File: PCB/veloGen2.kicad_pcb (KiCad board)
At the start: 2 copper layers, 67 x 24 mm, 43 parts, among them J1 Conn_01x06, J2 Gen. IN, J3 Bat, Q3 STL6N3LLH6, T1 MSD1260, U1 ESP-WROOM-32, U2 TS1101, U4 MAX8881, U5 MCP1630

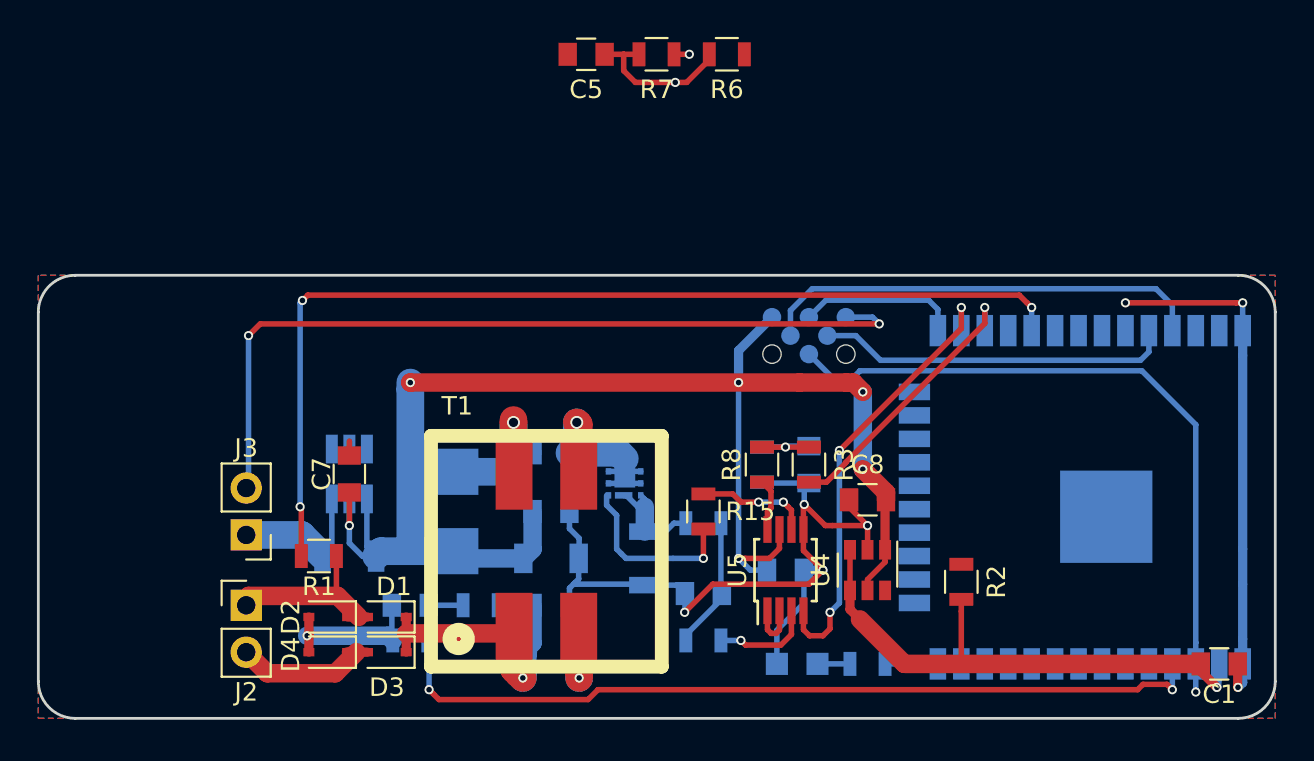
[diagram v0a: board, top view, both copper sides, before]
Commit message: moved stuff around 0.6 vias
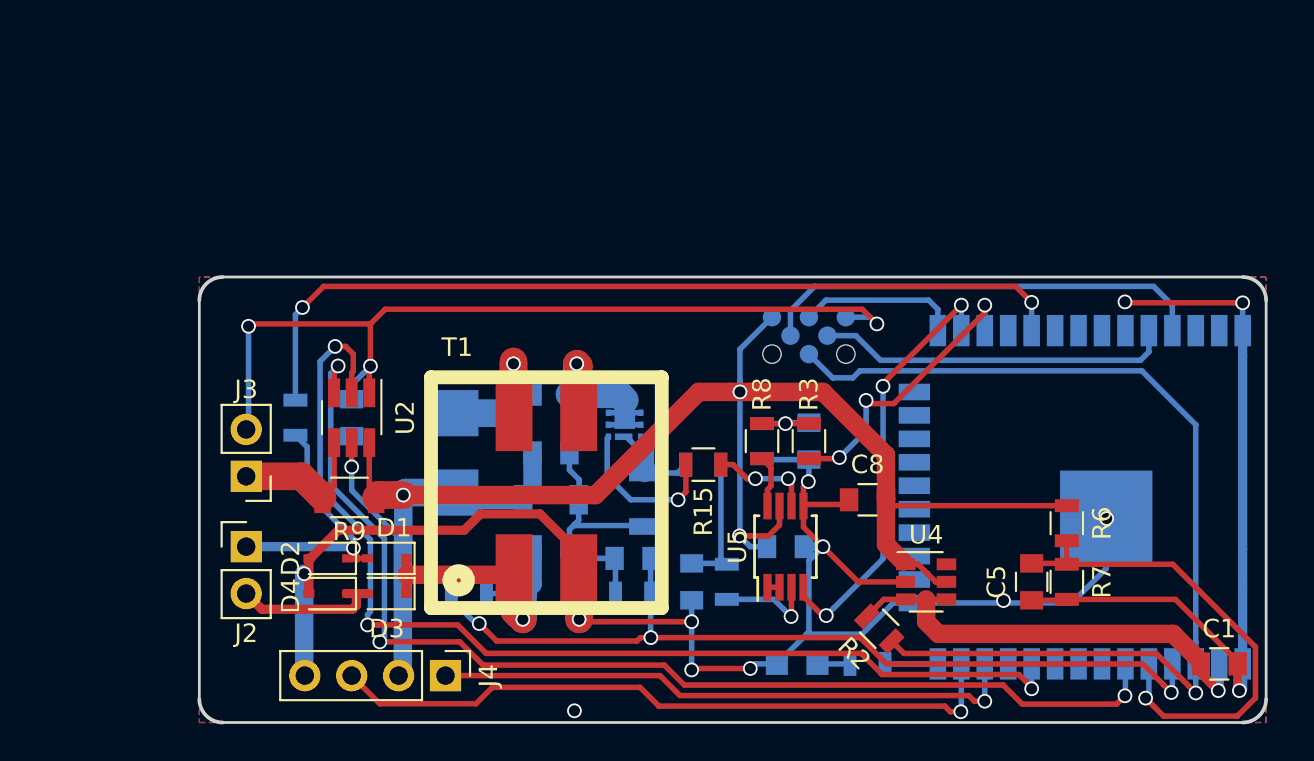
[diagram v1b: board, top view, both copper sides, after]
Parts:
- added J4: Conn_01x04, Socket_Strips:Socket_Strip_Straight_1x04_Pitch2.54mm, F.Cu at (59.1, 146.7)
- C7, R1: moved to B.Cu
- R9, U2: moved to F.Cu
- moved C5 37.4 mm to (90.8, 141.6), turned to 270 degrees
- moved R7 36.2 mm to (92.7, 141.6), turned to 270 degrees
- moved R6 31.4 mm to (92.7, 138.4), turned to 270 degrees
- moved C2 12.3 mm to (69.2, 140.3)
- moved R5 12.3 mm to (69.2, 142.2)
- moved R1 7.60 mm to (50.9, 132.7), turned to 90 degrees
- moved R2 5.12 mm to (82.5, 144.1), turned to 315 degrees
- moved R18 3.42 mm to (74.3, 141.6), turned to 270 degrees
- moved U4 3.24 mm to (85.1, 141.6), turned to 0 degrees
- moved C11 3.18 mm to (64.8, 139.7)
- moved C13 3.18 mm to (64.8, 131.4)
- moved C14 3.18 mm to (64.8, 137.2)
- moved J2 3.18 mm to (48.3, 139.7)
- moved J3 3.18 mm to (48.3, 135.9)
- moved R16 3.18 mm to (69.8, 137.2)
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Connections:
- U1 pad 12: Net-(U1-Pad12) -> /extSda
- U1 pad 13: Net-(U1-Pad13) -> /extScl
- U1 pad 30: /extScl -> Net-(U1-Pad30)
- U1 pad 31: /extSda -> Net-(U1-Pad31)
- U2 pad 4: +BATT -> Net-(J3-Pad1)
- U2 pad 6: Net-(J3-Pad1) -> +BATT
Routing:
- net GND: track 133.7 -> 196.0 mm, vias 12 -> 16
- net /IBatt: track 0.00 -> 61.6 mm, vias 0 -> 3
- net /IBattSign: track 0.00 -> 58.7 mm, vias 0 -> 3
- net /extScl: track 0.00 -> 37.1 mm, vias 0 -> 1
- net /extSda: track 0.00 -> 31.8 mm, vias 0 -> 1
- net /Vbatt: track 8.46 -> 26.7 mm
- net /rstBtn: track 37.4 -> 55.1 mm
- net +BATT: track 84.9 -> 99.0 mm, vias 6 -> 4
- net /speedPulse: track 55.1 -> 47.0 mm, vias 3 -> 2
- net +3V3: track 29.7 -> 24.9 mm
- net Net-(D1-Pad2): track 11.3 -> 15.1 mm, vias 0 -> 1
- net Net-(U5-Pad1): track 2.88 -> 0.65 mm
- net Net-(Q3-Pad1): track 9.63 -> 8.52 mm
- net /Vgen: track 48.8 -> 47.8 mm, vias 2 -> 3
- net /sepicPwm: track 24.4 -> 23.4 mm
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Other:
- board size 67 x 24 mm -> 57.8 x 24.1 mm
- net class Default: via_dia 0.5 -> 0.8; via_drill 0.3 -> 0.6
- rule via_min_drill: 0.3 -> 0.6
- rule via_min_size: 0.5 -> 0.8
